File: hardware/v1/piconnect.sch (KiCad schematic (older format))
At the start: 20 parts, among them CON1 BARREL_JACK, P1 CONN_01X04, P10 CONN_01X04, P11 CONN_01X04, P12 CONN_01X04, P13 CONN_02X05, P14 CONN_02X05, P15 CONN_02X05, P16 CONN_02X05, P17 CONN_02X05, P18 CONN_02X05, P2 CONN_01X04, P3 CONN_01X04, P4 CONN_01X04, P5 CONN_01X04, P6 CONN_01X04, P7 CONN_01X04, P8 CONN_01X04, P9 CONN_01X04, U1 Pi2_Connector

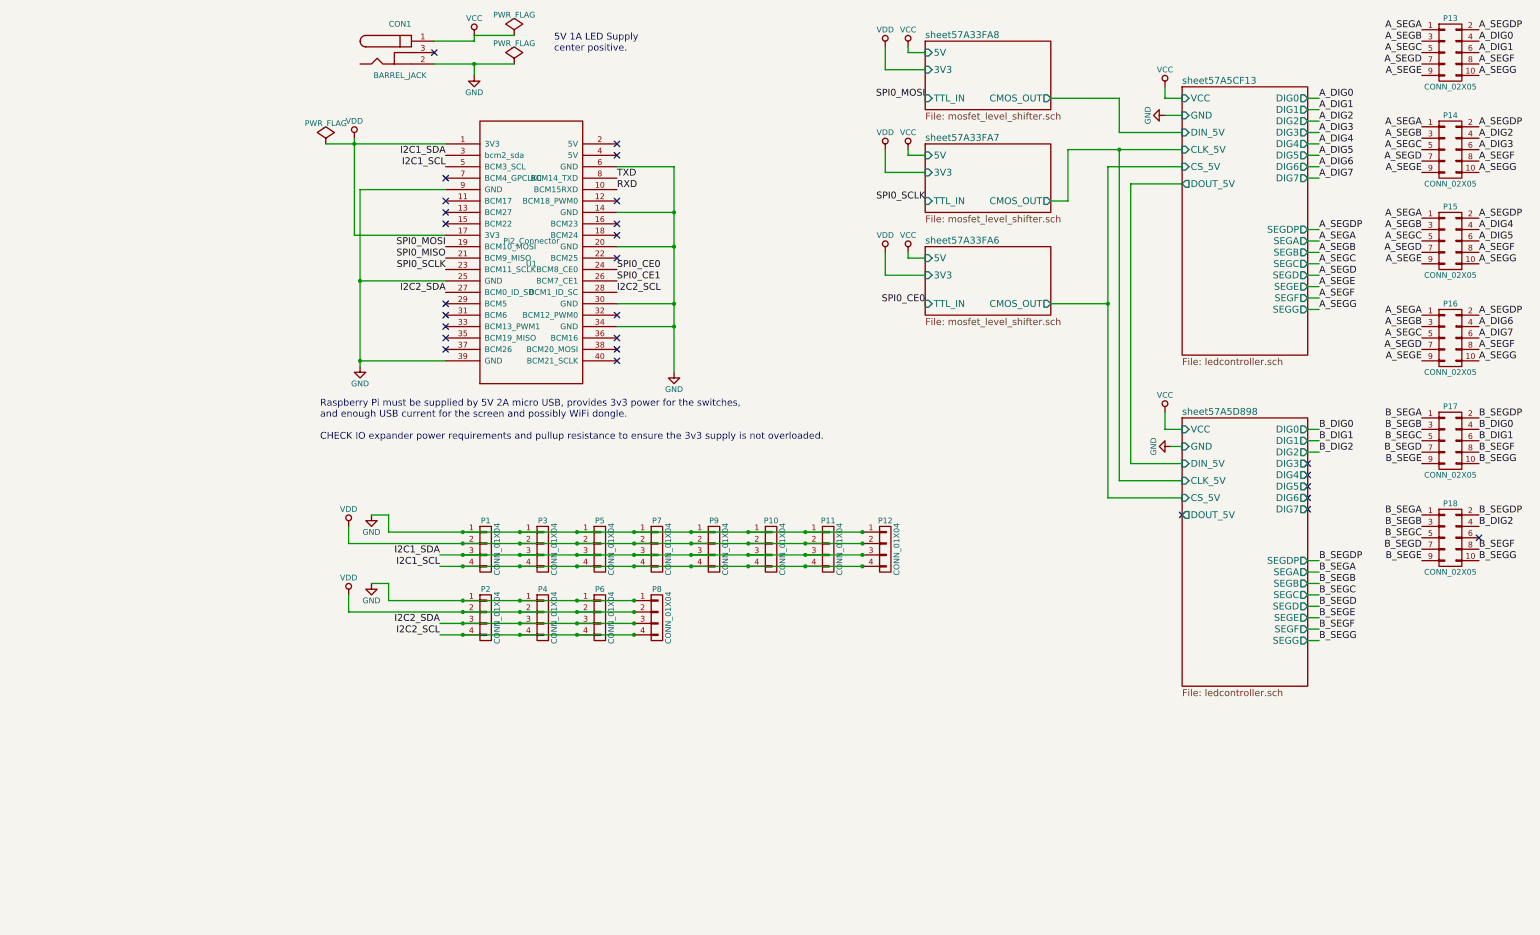
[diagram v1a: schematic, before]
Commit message: Correct footprints for barrel connector and rotary switch.
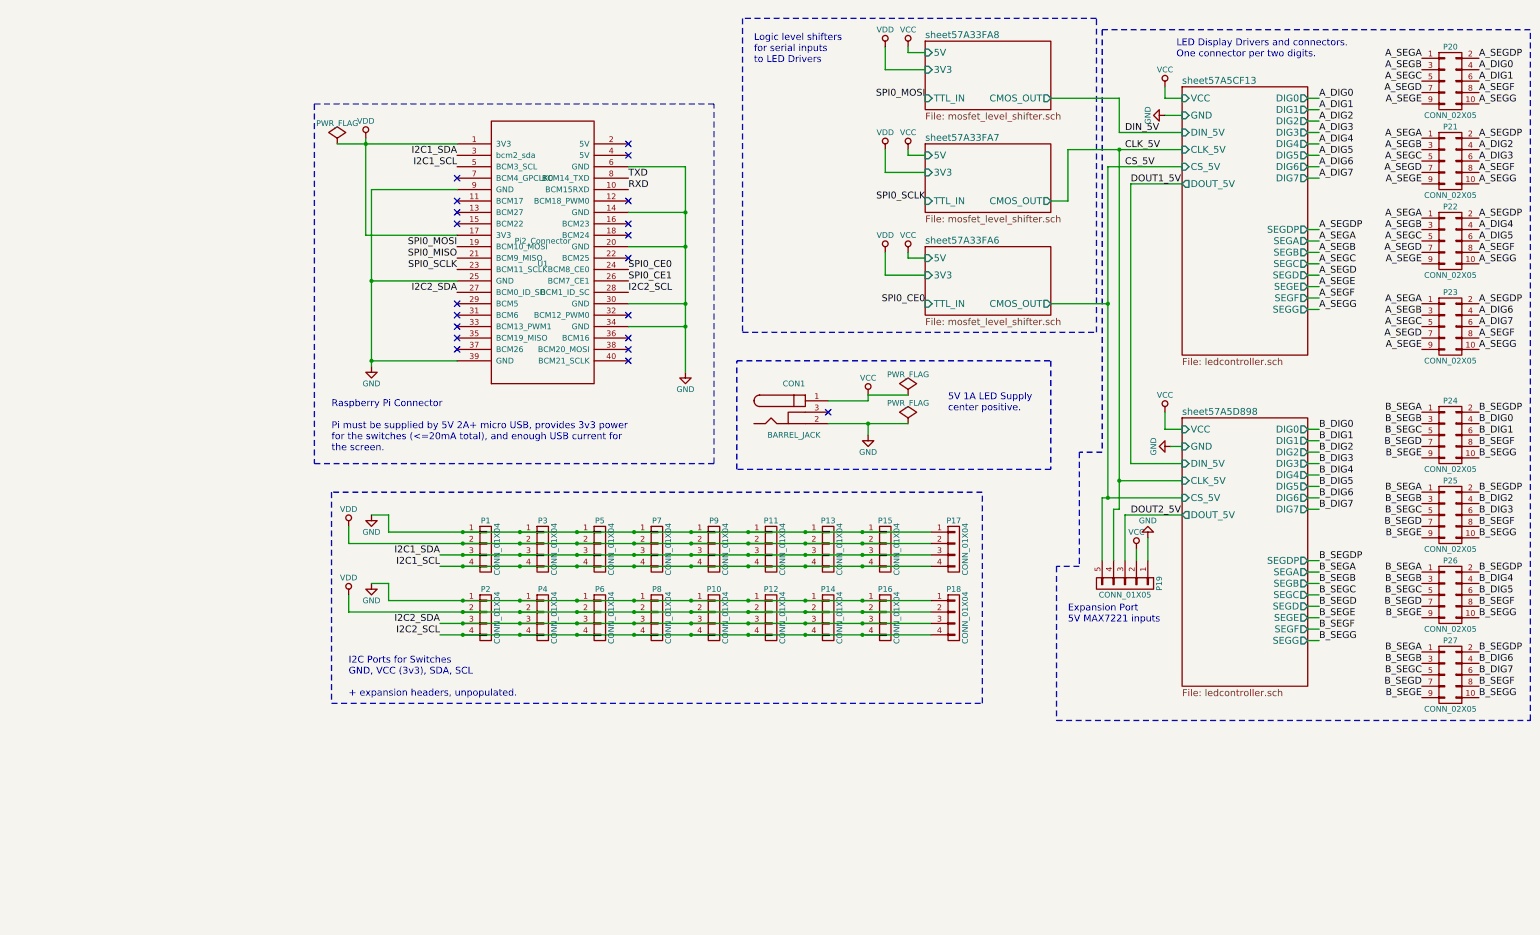
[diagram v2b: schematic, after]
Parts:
- added P10, P12, P14, P16, P17, P18: CONN_01X04, Pin_Headers:Pin_Header_Straight_1x04, symbol CONN_01X04
- added P19: CONN_01X05, Pin_Headers:Pin_Header_Straight_1x05, symbol CONN_01X05
- added P26, P27: CONN_02X05, Pin_Headers:Pin_Header_Straight_2x05, symbol CONN_02X05
- CON1: footprint (none) -> Connect:BARREL_JACK
- renumbered P10 to P11, P11 to P13, P12 to P15, P13 to P20, P14 to P21, P15 to P22, P16 to P23, P17 to P24, P18 to P25
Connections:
- net B_SEGA: now also P26.1 (P1), P27.1 (P1)
- net B_SEGB: now also P26.3 (P3), P27.3 (P3)
- net B_SEGC: now also P26.5 (P5), P27.5 (P5)
- net B_SEGD: now also P26.7 (P7), P27.7 (P7)
- net B_SEGDP: now also P26.2 (P2), P27.2 (P2)
- net B_SEGE: now also P26.9 (P9), P27.9 (P9)
- net B_SEGF: now also P26.8 (P8), P27.8 (P8)
- net B_SEGG: now also P26.10 (P10), P27.10 (P10)
- net GND: now also P10.1 (P1), P12.1 (P1), P14.1 (P1), P16.1 (P1), P17.1 (P1), P18.1 (P1), P19.1 (P1)
- net I2C1_SCL: now also P17.4 (P4)
- net I2C1_SDA: now also P17.3 (P3)
- net I2C2_SCL: now also P10.4 (P4), P12.4 (P4), P14.4 (P4), P16.4 (P4), P18.4 (P4)
- net I2C2_SDA: now also P10.3 (P3), P12.3 (P3), P14.3 (P3), P16.3 (P3), P18.3 (P3)
- net VCC: now also P19.2 (P2)
- net VDD: now also P10.2 (P2), P12.2 (P2), P14.2 (P2), P16.2 (P2), P17.2 (P2), P18.2 (P2)
- net B_DIG3: now reaches P25.6 (P6)
- new net B_DIG4: P26.4 (P4)
- new net B_DIG5: P26.6 (P6)
- new net B_DIG6: P27.4 (P4)
- new net B_DIG7: P27.6 (P6)
- new net CLK_5V: P19.4 (P4)
- new net CS_5V: P19.5 (P5)
- new net DOUT2_5V: P19.3 (P3)
- no-connect marks 27 -> 20
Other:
- note added: "Expansion Port\n5V MAX7221 inputs"
- note added: "I2C Ports for Switches\nGND, VCC (3v3), SDA, SCL\n\n+ expansion headers, unpopulated."
- note added: "LED Display Drivers and connectors.\nOne connector per two digits."
- note added: "Logic level shifters\nfor serial inputs\nto LED Drivers"
- note added: "Raspberry Pi Connector\n\nPi must be supplied by 5V 2A+ micro USB, provides 3v3 power\nfor the switches (<=20mA total), and enough USB current for\nthe screen."
- note removed: "Raspberry Pi must be supplied by 5V 2A micro USB, provides 3v3 power for the switches,\nand enough USB current for the screen and possibly WiFi dongle.\n\nCHECK IO expander power requirements and pullup resistance to ensure the 3v3 supply is not overloaded.\n"
- moved on the sheet: CON1, P20, P21, P23, P24, P25, U1

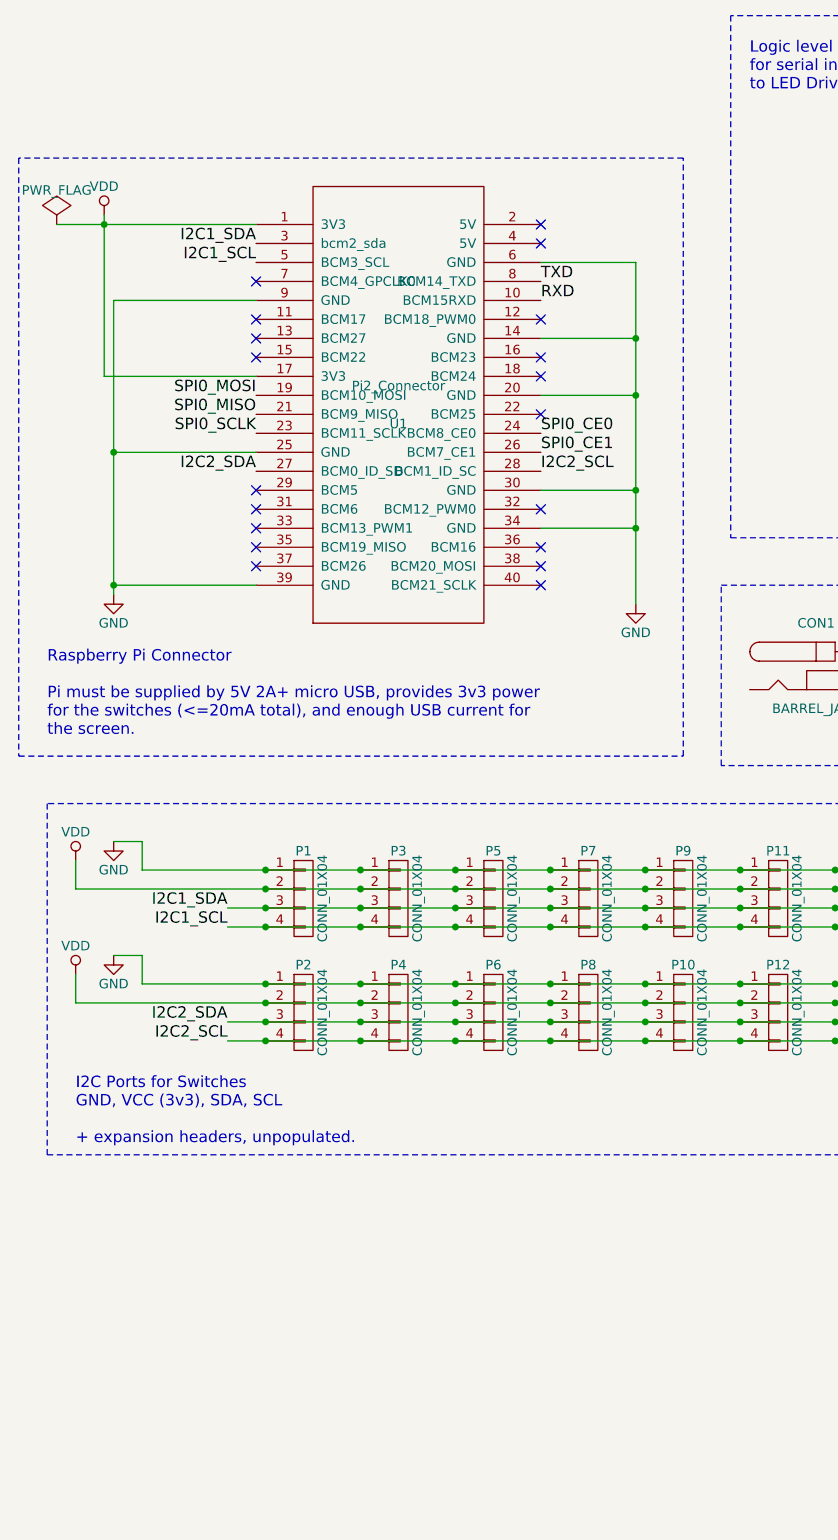
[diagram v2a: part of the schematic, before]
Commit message: Complete piconnect circuit and start routing.
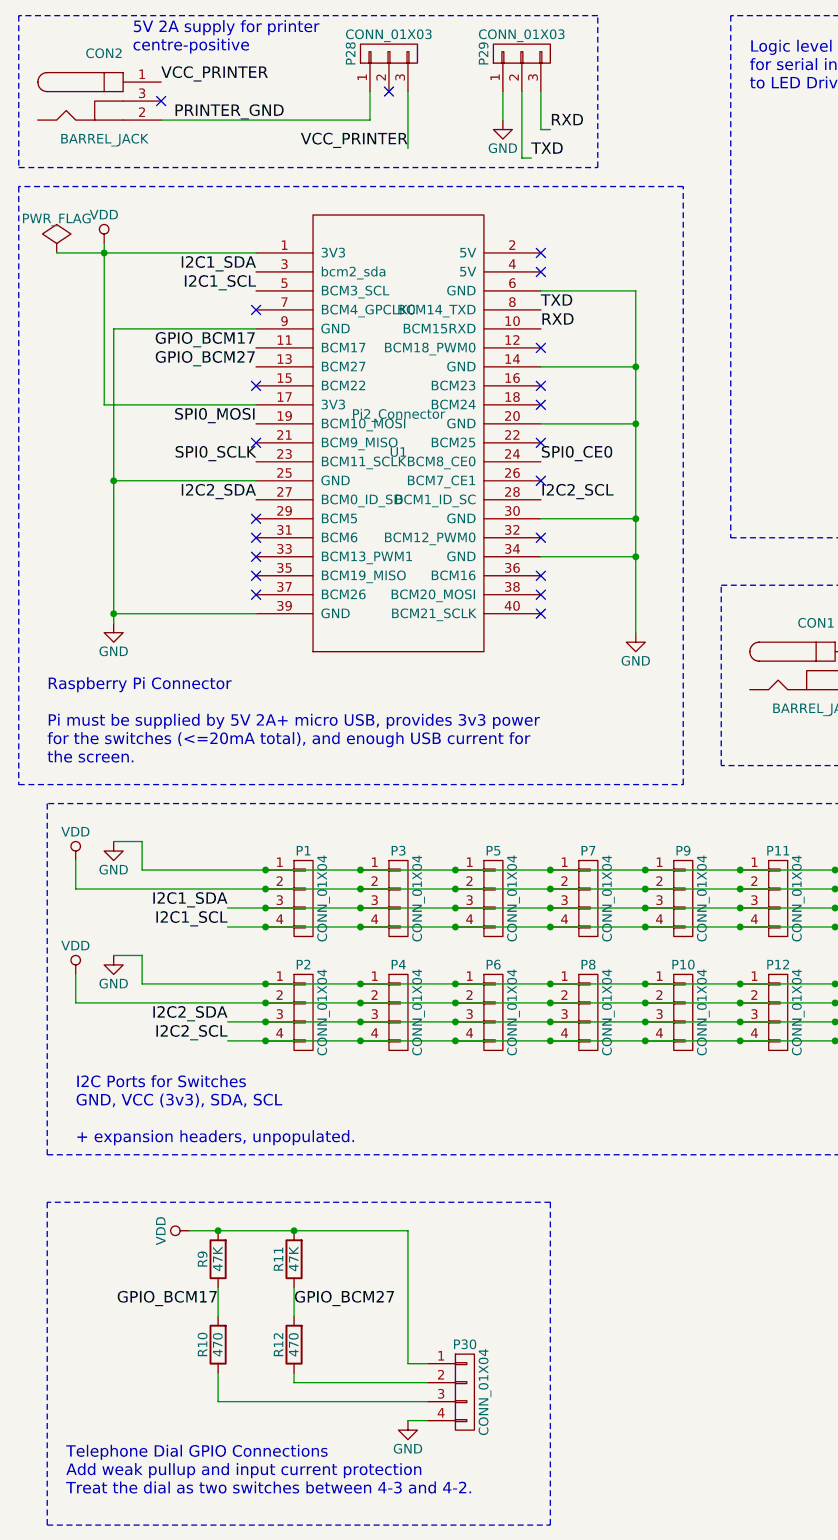
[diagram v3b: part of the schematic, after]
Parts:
- added CON2: BARREL_JACK, myparts:BARREL_JACK-custom, symbol BARREL_JACK
- added P28, P29: CONN_01X03, Pin_Headers:Pin_Header_Straight_1x03, symbol CONN_01X03
- added P30: CONN_01X04, Pin_Headers:Pin_Header_Straight_1x04, symbol CONN_01X04
- added R10, R12: 470, Resistors_ThroughHole:Resistor_Horizontal_RM10mm, symbol R
- added R11, R9: 47K, Resistors_ThroughHole:Resistor_Horizontal_RM10mm, symbol R
- CON1: footprint Connect:BARREL_JACK -> myparts:BARREL_JACK-custom
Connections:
- net GND: now also P29.1 (P1), P30.4 (P4)
- net RXD: now also P29.3 (P3)
- net TXD: now also P29.2 (P2)
- net VDD: now also P30.1 (P1), R11.2, R9.2
- net GPIO_BCM17: now reaches U1.11 (BCM17)
- net GPIO_BCM17: now also R10.2, R9.1
- net GPIO_BCM27: now reaches U1.13 (BCM27)
- net GPIO_BCM27: now also R11.1, R12.2
- net SPI0_CE1: no longer names the net of U1.26 (BCM7_CE1)
- net SPI0_MISO: no longer names the net of U1.21 (BCM9_MISO)
- new net: P30.2 (P2), R12.1
- new net: P30.3 (P3), R10.1
- new net PRINTER_GND: CON2.2, P28.1 (P1)
- new net VCC_PRINTER: CON2.1, P28.3 (P3)
- no-connect marks 20 -> 22
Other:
- note added: "5V 2A supply for printer\ncentre-positive"
- note added: "Telephone Dial GPIO Connections\nAdd weak pullup and input current protection\nTreat the dial as two switches between 4-3 and 4-2."
- moved on the sheet: U1

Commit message: Add mosfet clock gates to I2C connector rows - because addresses conflict and the second bus (I2C0) cannot be used safely on the raspberry pi.
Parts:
- added Q4, Q5: 2N7000, TO_SOT_Packages_THT:TO-92_Inline_Wide, symbol Q_NMOS_DGS
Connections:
- net I2C1_SCL: now also Q4.1 (D), Q5.1 (D); no longer P1.4 (P4), P11.4 (P4), P13.4 (P4), P15.4 (P4), P17.4 (P4), P3.4 (P4), P5.4 (P4), P7.4 (P4), P9.4 (P4)
- net I2C1_SDA: now also P10.3 (P3), P12.3 (P3), P14.3 (P3), P16.3 (P3), P18.3 (P3), P2.3 (P3), P4.3 (P3), P6.3 (P3), P8.3 (P3)
- net EN_I2C0_1: now reaches U1.29 (BCM5)
- net EN_I2C0_1: now also Q4.2 (G)
- net EN_I2C0_2: now reaches U1.31 (BCM6)
- net EN_I2C0_2: now also Q5.2 (G)
- net I2C2_SCL: no longer names the net of P10.4 (P4), P12.4 (P4), P14.4 (P4), P16.4 (P4), P18.4 (P4), P2.4 (P4), P4.4 (P4), P6.4 (P4), P8.4 (P4)
- net I2C2_SCL: now also Q5.3 (S); no longer U1.28 (BCM1_ID_SC)
- removed net I2C2_SDA: P10.3 (P3), P12.3 (P3), P14.3 (P3), P16.3 (P3), P18.3 (P3), P2.3 (P3), P4.3 (P3), P6.3 (P3), P8.3 (P3), U1.27 (BCM0_ID_SD)
- new net: P1.4 (P4), P11.4 (P4), P13.4 (P4), P15.4 (P4), P17.4 (P4), P3.4 (P4), P5.4 (P4), P7.4 (P4), P9.4 (P4), Q4.3 (S)
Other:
- note added: "Primitive clock gating for enabling one of the two\nsets of ICs on conflicting I2C addresses."
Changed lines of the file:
@@
 LIBS:contrib
 LIBS:valves
-LIBS:Pi2_Connector
-LIBS:MAX7221
-LIBS:MCP23S17
-LIBS:MCP23017
 LIBS:piconnect-cache
 EELAYER 25 0
@@
 Text Label 1800 2000 2    60   ~ 0
 I2C1_SCL
-Text Label 1800 3100 2    60   ~ 0
-I2C2_SDA
-Text Label 3300 3100 0    60   ~ 0
-I2C2_SCL
 Text Label 1800 2700 2    60   ~ 0
 SPI0_MOSI
@@
 NoConn ~ 1800 3600
 NoConn ~ 1800 3400
-NoConn ~ 1800 3300
-NoConn ~ 1800 3200
 NoConn ~ 1800 2500
 NoConn ~ 1800 2100
-Text Label 1650 5850 2    60   ~ 0
-I2C2_SDA
-Text Label 1650 5950 2    60   ~ 0
-I2C2_SCL
 Text Label 1650 5250 2    60   ~ 0
 I2C1_SDA
-Text Label 1650 5350 2    60   ~ 0
+Text Label -425 4900 0    60   ~ 0
 I2C1_SCL
 $Comp
 L VDD #PWR019
 U 1 1 57A9D16C
-P 850 5000
-F 0 "#PWR019" H 850 4850 50  0001 C CNN
-F 1 "VDD" H 850 5150 50  0000 C CNN
-F 2 "" H 850 5000 50  0000 C CNN
-F 3 "" H 850 5000 50  0000 C CNN
-	1    850  5000
+P 850 5150
+F 0 "#PWR019" H 850 5000 50  0001 C CNN
+F 1 "VDD" H 850 5300 50  0000 C CNN
+F 2 "" H 850 5150 50  0000 C CNN
+F 3 "" H 850 5150 50  0000 C CNN
+	1    850  5150
 	1    0    0    -1
 $EndComp
@@
 $EndComp
 $Comp
-L VDD #PWR021
-U 1 1 57AA1B7B
-P 850 5600
-F 0 "#PWR021" H 850 5450 50  0001 C CNN
-F 1 "VDD" H 850 5750 50  0000 C CNN
-F 2 "" H 850 5600 50  0000 C CNN
-F 3 "" H 850 5600 50  0000 C CNN
-	1    850  5600
-	1    0    0    -1
-$EndComp
-$Comp
-L GND #PWR022
+L GND #PWR021
 U 1 1 57AA1B81
 P 1050 5500
-F 0 "#PWR022" H 1050 5250 50  0001 C CNN
+F 0 "#PWR021" H 1050 5250 50  0001 C CNN
 F 1 "GND" H 1050 5350 50  0000 C CNN
 F 2 "" H 1050 5500 50  0000 C CNN
@@
 $EndComp
 $Comp
-L GND #PWR023
+L GND #PWR022
 U 1 1 57ADEFF2
 P 7850 5100
-F 0 "#PWR023" H 7850 4850 50  0001 C CNN
+F 0 "#PWR022" H 7850 4850 50  0001 C CNN
 F 1 "GND" H 7850 4950 50  0000 C CNN
 F 2 "" H 7850 5100 50  0000 C CNN
@@
 $EndComp
 $Comp
-L VCC #PWR024
+L VCC #PWR023
 U 1 1 57ADF192
 P 7750 5200
-F 0 "#PWR024" H 7750 5050 50  0001 C CNN
+F 0 "#PWR023" H 7750 5050 50  0001 C CNN
 F 1 "VCC" H 7750 5350 50  0000 C CNN
 F 2 "" H 7750 5200 50  0000 C CNN
@@
 NoConn ~ 1300 1000
 $Comp
-L GND #PWR026
+L GND #PWR024
 U 1 1 57ADD7D4
 P 3100 1100
-F 0 "#PWR026" H 3100 850 50  0001 C CNN
+F 0 "#PWR024" H 3100 850 50  0001 C CNN
 F 1 "GND" H 3100 950 50  0000 C CNN
 F 2 "" H 3100 1100 50  0000 C CNN
@@
 5V 2A supply for printer\ncentre-positive
 $Comp
-L VDD #PWR027
+L VDD #PWR025
 U 1 1 57AE1E9A
 P 1450 6950
-F 0 "#PWR027" H 1450 6800 50  0001 C CNN
+F 0 "#PWR025" H 1450 6800 50  0001 C CNN
 F 1 "VDD" H 1450 7100 50  0000 C CNN
 F 2 "" H 1450 6950 50  0000 C CNN
@@
 GPIO_BCM27
 $Comp
-L GND #PWR028
+L GND #PWR026
 U 1 1 57AE271C
 P 2600 7950
-F 0 "#PWR028" H 2600 7700 50  0001 C CNN
+F 0 "#PWR026" H 2600 7700 50  0001 C CNN
 F 1 "GND" H 2600 7800 50  0000 C CNN
 F 2 "" H 2600 7950 50  0000 C CNN
@@
 	1200 4900 1050 4900
 Connection ~ 1850 5050
-Wire Wire Line
-	850  5000 850  5150
 Connection ~ 1850 5150
 Wire Wire Line
@@
 	1650 5250 5950 5250
 Wire Wire Line
-	1650 5350 5950 5350
+	-425 5350 5950 5350
 Connection ~ 2350 5250
 Connection ~ 2350 5350
@@
 	1200 5500 1050 5500
 Connection ~ 1850 5650
-Wire Wire Line
-	850  5600 850  5750
 Connection ~ 1850 5750
 Connection ~ 2350 5850
@@
 	1200 5650 5950 5650
 Wire Wire Line
-	850  5750 5950 5750
-Wire Wire Line
 	1650 5850 5950 5850
 Wire Wire Line
-	1650 5950 5950 5950
+	-425 5950 5950 5950
 Connection ~ 3850 5850
 Connection ~ 3850 5950
@@
 Text Label 1950 1100 2    60   ~ 0
 PRINTER_GND
+NoConn ~ 1800 3100
+NoConn ~ 3300 3100
+Text Label 1800 3200 2    60   ~ 0
+EN_I2C0_1
+Text Label 1800 3300 2    60   ~ 0
+EN_I2C0_2
+Text Label -725 5100 2    60   ~ 0
+EN_I2C0_1
+Text Label -725 5725 2    60   ~ 0
+EN_I2C0_2
+Text Label 1650 5850 2    60   ~ 0
+I2C1_SDA
+Text Label -425 5525 0    60   ~ 0
+I2C1_SCL
+Wire Wire Line
+	-425 5350 -425 5300
+Wire Wire Line
+	-425 5950 -425 5925
+$Comp
+L VDD #PWR027
+U 1 1 57AFF7A4
+P 900 5750
+F 0 "#PWR027" H 900 5600 50  0001 C CNN
+F 1 "VDD" H 900 5900 50  0000 C CNN
+F 2 "" H 900 5750 50  0000 C CNN
+F 3 "" H 900 5750 50  0000 C CNN
+	1    900  5750
+	1    0    0    -1
+$EndComp
+Wire Wire Line
+	900  5750 5950 5750
+Text Notes -2075 6200 0    60   ~ 0
+Primitive clock gating for enabling one of the two\nsets of ICs on conflicting I2C addresses.
+Wire Notes Line
+	325  4800 325  6300
+Wire Notes Line
+	325  6300 -2125 6300
+Wire Notes Line
+	-2125 6300 -2125 4800
+Wire Notes Line
+	-2125 4800 350  4800
+$Comp
+L Q_NMOS_DGS Q5
+U 1 1 57AFE892
+P -525 5725
+F 0 "Q5" H -225 5775 50  0000 R CNN
+F 1 "2N7000" H 125 5675 50  0000 R CNN
+F 2 "TO_SOT_Packages_THT:TO-92_Inline_Wide" H -325 5825 50  0001 C CNN
+F 3 "" H -525 5725 50  0000 C CNN
+	1    -525 5725
+	1    0    0    -1
+$EndComp
+$Comp
+L Q_NMOS_DGS Q4
+U 1 1 57AFEA73
+P -525 5100
+F 0 "Q4" H -225 5150 50  0000 R CNN
+F 1 "2N7000" H 125 5050 50  0000 R CNN
+F 2 "TO_SOT_Packages_THT:TO-92_Inline_Wide" H -325 5200 50  0001 C CNN
+F 3 "" H -525 5100 50  0000 C CNN
+	1    -525 5100
+	1    0    0    -1
+$EndComp
 $EndSCHEMATC
